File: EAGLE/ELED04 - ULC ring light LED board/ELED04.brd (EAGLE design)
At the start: 60 x 60 mm, 39 parts, among them J7 RINGLIGHT

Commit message: On the two ring light boards, I changed the LEDs from 1206 package to 1210 in order to accomodate a brighter LED.
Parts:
- LED1, LED10, LED11, LED12, LED13, LED14, LED15, LED16, LED2, LED3, LED4, LED5, LED6, LED7, LED8, LED9: device SparkFun-LED:LED-1206-NO_SILK -> GinWhiskers - temp stuff:DIODE-1210
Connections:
- net LED-: now also LED12.K, LED16.K, LED4.K, LED8.K; no longer LED12.C, LED16.C, LED4.C, LED8.C
- net N$1: now also LED1.K; no longer LED1.C
- net N$12: now also LED9.K; no longer LED9.C
- net N$13: now also LED5.K; no longer LED5.C
- net N$14: now also LED11.K; no longer LED11.C
- net N$17: now also LED13.K; no longer LED13.C
- net N$19: now also LED15.K; no longer LED15.C
- net N$3: now also LED3.K; no longer LED3.C
- net N$4: now also LED7.K; no longer LED7.C
- net N$6: now also LED2.K; no longer LED2.C
- net N$7: now also LED6.K; no longer LED6.C
- net N$8: now also LED10.K; no longer LED10.C
- net N$9: now also LED14.K; no longer LED14.C
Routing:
- net LED+: track 175.5 -> 179.9 mm
- net LED-: track 171.4 -> 168.9 mm

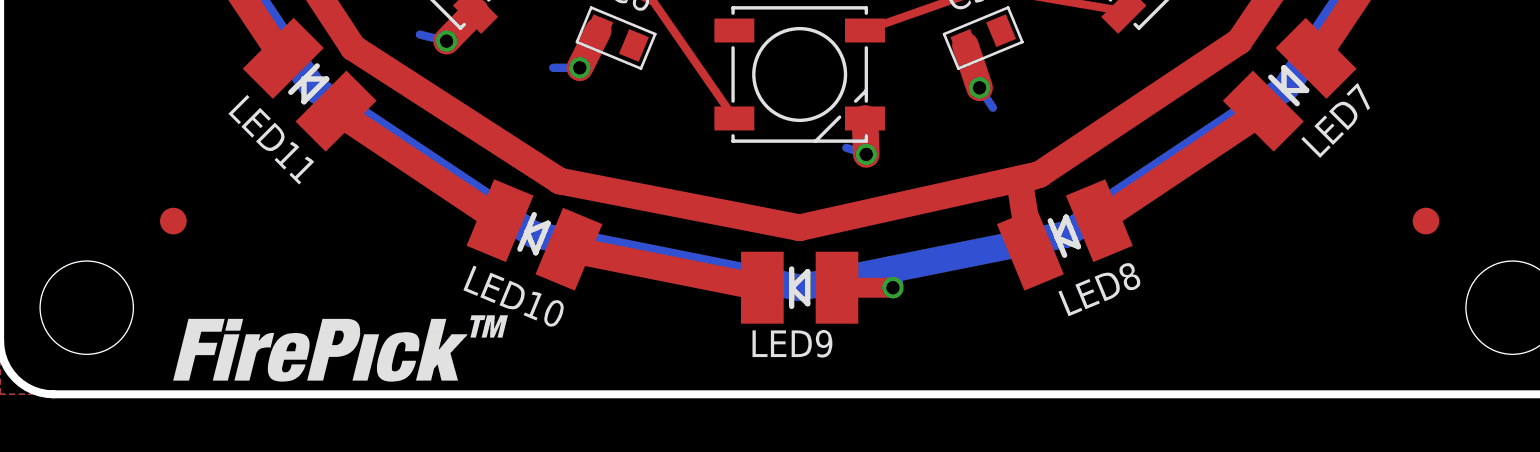
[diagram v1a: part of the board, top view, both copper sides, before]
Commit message: Added frames, logos, part numbers, and fiducials
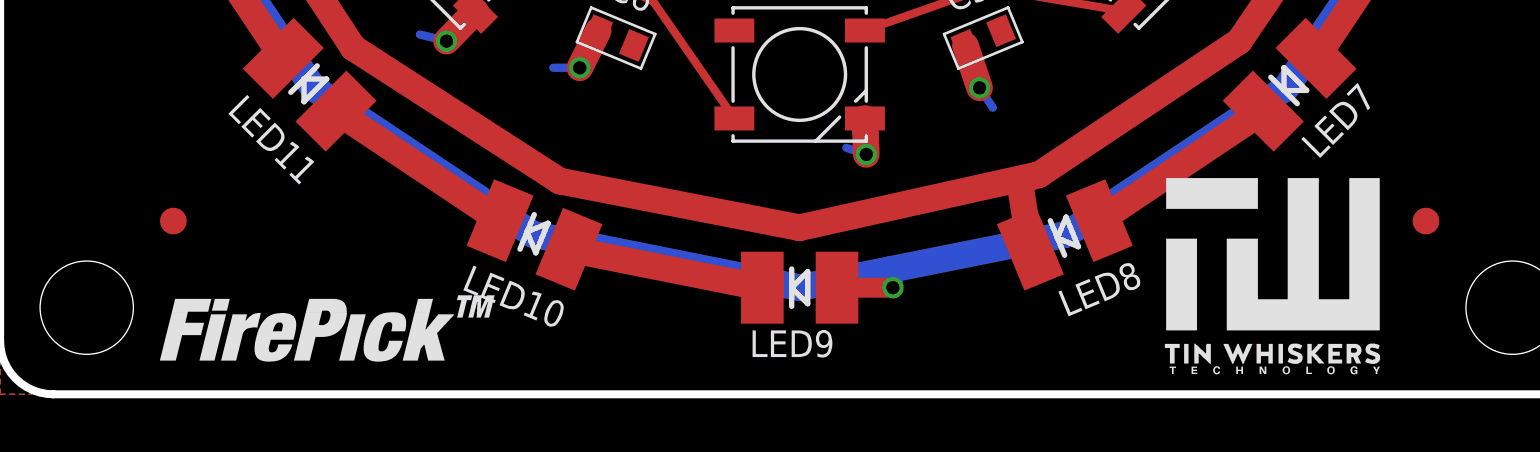
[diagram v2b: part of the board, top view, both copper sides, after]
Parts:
- removed U$1: TIN-WHISKERSSMALL, !tin-whiskers:TIN-WHISKERS-SMALL
- added U$3: TIN-WHISKERSSMALL, !tin-whiskers-logo:TIN-WHISKERS-SMALL
- moved LOGO4 0.90 mm to (-24.0, -28.8)
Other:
- board text added: "ELED04 Rev --"
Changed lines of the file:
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@@
 <layer number="20" name="Dimension" color="15" fill="1" visible="yes" active="yes"/>
 <layer number="21" name="tPlace" color="7" fill="1" visible="yes" active="yes"/>
-<layer number="22" name="bPlace" color="7" fill="1" visible="no" active="yes"/>
+<layer number="22" name="bPlace" color="7" fill="1" visible="yes" active="yes"/>
 <layer number="23" name="tOrigins" color="15" fill="1" visible="yes" active="yes"/>
 <layer number="24" name="bOrigins" color="15" fill="1" visible="no" active="yes"/>
@@
 AREA AWAY!</text>
 <circle x="0" y="21.5" radius="1.4142125" width="0.3048" layer="51"/>
+<text x="-12.25" y="27.5" size="1" layer="22" font="vector" ratio="11" rot="MR0">ELED04 Rev --</text>
 </plain>
 <attributes>
@@
 <element name="FID3" library="SparkFun-Aesthetics" package="FIDUCIAL-1X2" value="FIDUCIAL1X2" x="-23.5" y="-23.5" smashed="yes"/>
 <element name="FID4" library="SparkFun-Aesthetics" package="FIDUCIAL-1X2" value="FIDUCIAL1X2" x="23.5" y="23.5" smashed="yes"/>
-<element name="LOGO4" library="FirePick" package="LOGO-FIREPICK-MEDIUM" value="LOGO-FIREPICKMEDIUM" x="-23.5" y="-29.5" smashed="yes">
-<attribute name="DNP" value="T" x="-23.5" y="-29.5" size="1.778" layer="27" display="off"/>
-<attribute name="BOM" value="EXCLUDE" x="-23.5" y="-29.5" size="1.778" layer="27" display="off"/>
+<element name="LOGO4" library="FirePick" package="LOGO-FIREPICK-MEDIUM" value="LOGO-FIREPICKMEDIUM" x="-24" y="-28.75" smashed="yes">
+<attribute name="DNP" value="T" x="-24" y="-28.75" size="1.778" layer="27" display="off"/>
+<attribute name="BOM" value="EXCLUDE" x="-24" y="-28.75" size="1.778" layer="27" display="off"/>
 </element>
 <element name="LED13" library="GinWhiskers - temp stuff" package="DIODE-1210" value="WHITE" x="-26" y="0" smashed="yes" rot="R90">
@@
 <attribute name="PARTNO" value="LTST-C150CKT" x="-9.95" y="24.021" size="1.778" layer="27" rot="R22.5" display="off"/>
 </element>
-<element name="U$1" library="!tin-whiskers" package="TIN-WHISKERS-SMALL" value="TIN-WHISKERSSMALL" x="-8.5" y="14" smashed="yes" rot="MR0"/>
 <element name="J7" library="TinWhiskers" package="CON-JST-PH-2.0MM-5P-SMT-VRT" value="RINGLIGHT" x="0" y="18" smashed="yes" rot="MR0">
 <attribute name="NAME" x="6" y="26" size="1" layer="26" font="vector" ratio="11" rot="MR0"/>
@@
 <attribute name="NAME" x="-6.618234375" y="14.391465625" size="1" layer="25" font="vector" ratio="11" rot="R22.5"/>
 </element>
+<element name="U$3" library="!tin-whiskers-logo" package="TIN-WHISKERS-SMALL" value="TIN-WHISKERSSMALL" x="13.25" y="-29.5"/>
 </elements>
 <signals>

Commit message: Replaced fiducials with newer fiducials that have keepouts / restrict layers
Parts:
- FID1, FID2, FID3, FID4: value FIDUCIAL1X2 -> FIDUCIAL; device SparkFun-Aesthetics:FIDUCIAL-1X2 -> TinWhiskers:FIDUCIAL
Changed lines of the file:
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@@
 <attribute name="PARTNO" value="LTST-C150CKT" x="-24.021" y="-9.95" size="1.778" layer="27" rot="R112.5" display="off"/>
 </element>
-<element name="FID1" library="SparkFun-Aesthetics" package="FIDUCIAL-1X2" value="FIDUCIAL1X2" x="-23.5" y="23.5" smashed="yes"/>
-<element name="FID2" library="SparkFun-Aesthetics" package="FIDUCIAL-1X2" value="FIDUCIAL1X2" x="23.5" y="-23.5" smashed="yes"/>
-<element name="FID3" library="SparkFun-Aesthetics" package="FIDUCIAL-1X2" value="FIDUCIAL1X2" x="-23.5" y="-23.5" smashed="yes"/>
-<element name="FID4" library="SparkFun-Aesthetics" package="FIDUCIAL-1X2" value="FIDUCIAL1X2" x="23.5" y="23.5" smashed="yes"/>
+<element name="FID1" library="TinWhiskers" package="FIDUCIAL" value="FIDUCIAL" x="-23.5" y="23.5" smashed="yes"/>
+<element name="FID2" library="TinWhiskers" package="FIDUCIAL" value="FIDUCIAL" x="23.5" y="-23.5" smashed="yes"/>
+<element name="FID3" library="TinWhiskers" package="FIDUCIAL" value="FIDUCIAL" x="-23.5" y="-23.5" smashed="yes"/>
+<element name="FID4" library="TinWhiskers" package="FIDUCIAL" value="FIDUCIAL" x="23.5" y="23.5" smashed="yes"/>
 <element name="LOGO4" library="FirePick" package="LOGO-FIREPICK-MEDIUM" value="LOGO-FIREPICKMEDIUM" x="-24" y="-28.75" smashed="yes">
 <attribute name="DNP" value="T" x="-24" y="-28.75" size="1.778" layer="27" display="off"/>
